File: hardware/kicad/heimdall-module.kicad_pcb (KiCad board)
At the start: 2 copper layers, 54.9 x 30.1 mm, 29 parts, among them J2 Breakout, U1 MC33269DT-3.3G, U2 ESP32-C3-WROOM-02-N4, U3 TYPEC-214-ARP14H105, U4 USBLC6-2SC6

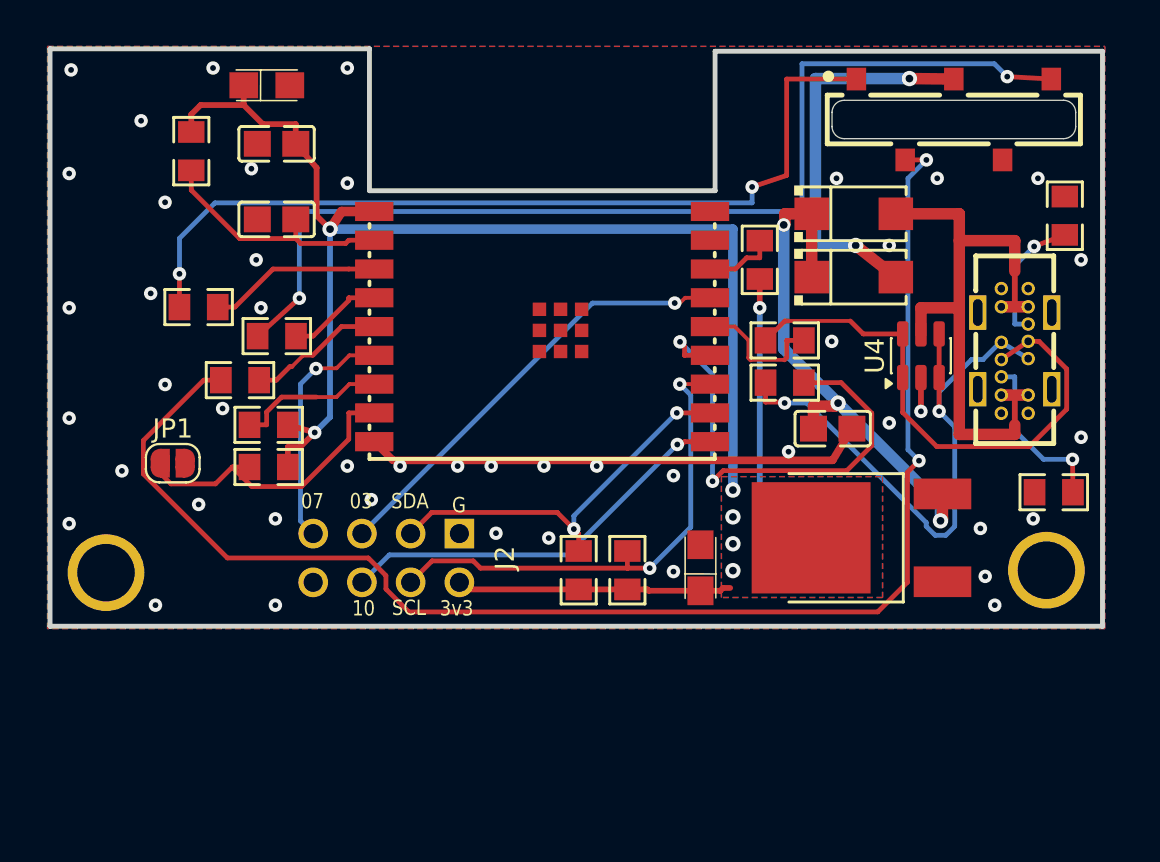
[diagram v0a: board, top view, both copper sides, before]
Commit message: Bay interface: Schottky isolation on all bay signal lines
The bay lines no longer connect straight to the ESP32 through 220R
(R5-R7 removed). Each line goes through a BAT54WS (D3-D6), the same
scheme as the DIY Multiprotocol module: the radio can only pull a line
low, and every high level comes from 3V3 pull-ups. A radio driving 5V
can't reach the ESP32.

- PPM in: D3 + R14 4.7k -> IO4
- DATA (CRSF, half duplex): RX D4 + R16 4.7k -> IO5, TX D5 <- IO6,
  R17 1.5k bay-side pull-up for fast rising edges
- HB out: D6 <- IO7, R15 4.7k bay-side pull-up
- Breakout J2 pin 7: IO7 -> IO1 (silk relabelled)

Board re-routed (prep -> Freerouting -> finish pipeline). DRC: 0 errors,
0 unconnected, 0 parity; only the known U3 A1 starved-thermal warning.

Co-Authored-By: Claude Opus 5.5 <noreply@anthropic.com>
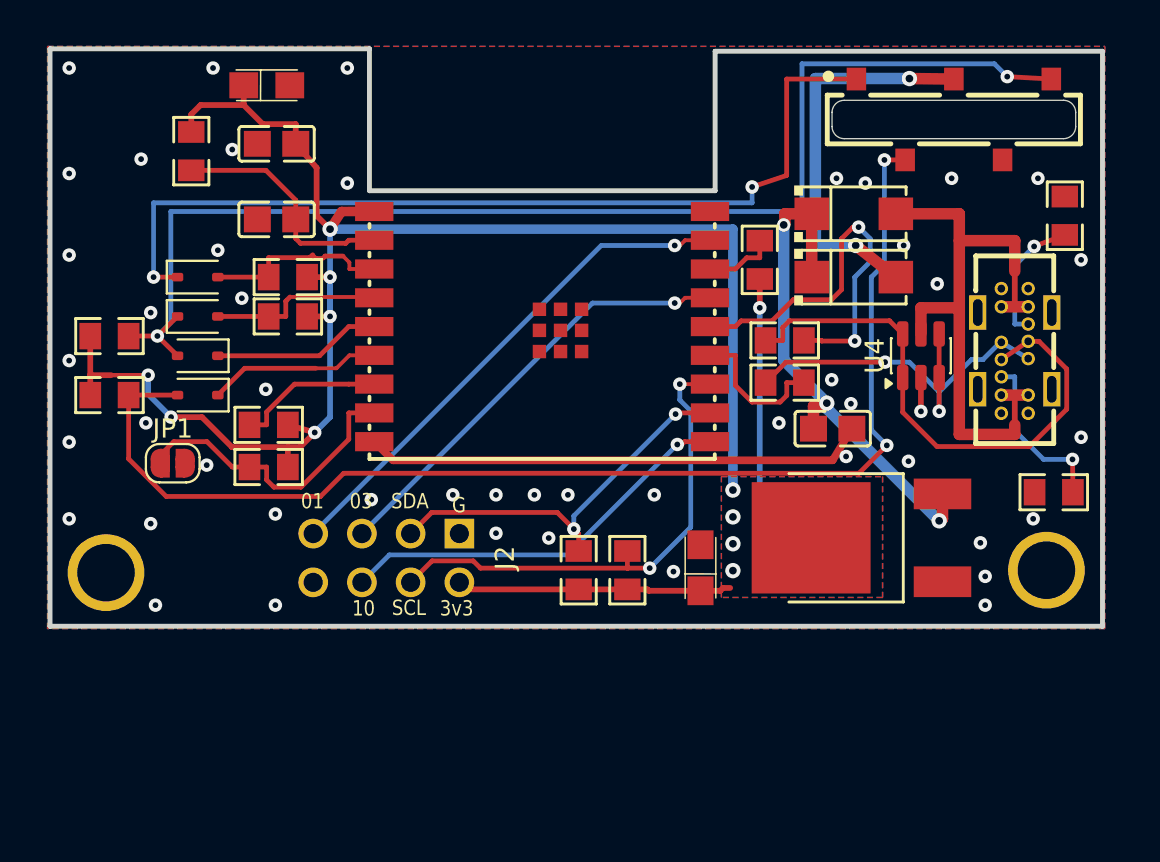
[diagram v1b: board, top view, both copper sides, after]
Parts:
- removed R5, R6, R7: 220Ω, heimdall-m-easyedapro:R0805
- added D3: BAT54WS, Diode_SMD:D_SOD-323, F.Cu at (127.7, 101.9)
- added D4: BAT54WS, Diode_SMD:D_SOD-323, F.Cu at (127.7, 104.0)
- added D5: BAT54WS, Diode_SMD:D_SOD-323, F.Cu at (127.7, 106.0)
- added D6: BAT54WS, Diode_SMD:D_SOD-323, F.Cu at (127.7, 108.0)
- added R14: 4.7kΩ, heimdall-m-easyedapro:R0805, F.Cu at (132.4, 101.9)
- added R15: 4.7kΩ, heimdall-m-easyedapro:R0805, F.Cu at (123.1, 108.0)
- added R16: 4.7kΩ, heimdall-m-easyedapro:R0805, F.Cu at (132.4, 104.0)
- added R17: 1.5kΩ, heimdall-m-easyedapro:R0805, F.Cu at (123.1, 105.0)
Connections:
- J2 pad 7: /IO7 -> /IO1
- U2 pad 17: unconnected-(U2-IO1-Pad17) -> /IO1
- U2 pad 3: Net-(U2-IO4) -> /PPM_IN
- U2 pad 4: Net-(U2-IO5) -> /DATA_RX
- U2 pad 5: Net-(U2-IO6) -> /DATA_TX
- U2 pad 6: /IO7 -> /HB_OUT
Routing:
- net /IO1: track 0.00 -> 27.0 mm, vias 0 -> 1
- net /VCC: track 91.7 -> 111.6 mm, vias 7 -> 11
- net Net-(U2-IO18): track 25.1 -> 7.64 mm, vias 2 -> 0
- net Net-(U2-IO19): track 7.09 -> 20.6 mm, vias 0 -> 2
- net /IO7: track 12.5 -> 0.00 mm, vias 1 -> 0
- net /HB: track 75.0 -> 63.9 mm
- net /DATA: track 54.6 -> 65.1 mm
- net /USB-D-: track 31.4 -> 21.1 mm
- net /PPM_IN: track 0.00 -> 9.82 mm
- net /DATA_RX: track 0.00 -> 9.08 mm
- net /HB_OUT: track 0.00 -> 9.01 mm
- net Net-(U2-IO4): track 8.98 -> 0.00 mm
- net /DATA_TX: track 0.00 -> 8.78 mm
- net Net-(U2-IO6): track 7.16 -> 0.00 mm
- net Net-(U2-IO5): track 4.99 -> 0.00 mm
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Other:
- board text added: "01"
- board text removed: "07"

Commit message: Bay DATA transmit through a 5V-tolerant buffer: S.Port and CRSF
The module has to talk S.Port (idle low, inverted) or CRSF (idle high)
on the DATA pin depending on what the internal module uses. The
pull-low-only diode and the 1.5k pull-up only worked for CRSF.

- D5 and the 1.5k pull-up out; U5 74LVC1G34 (always on) + R17 1k in.
  The UART idle level holds the line in either mode; the radio
  overrides 1k when it transmits.
- DATA_TX on IO7, HB_OUT on IO8 (R12 doubles as its pull-up), IO6 free.
- D6/R15 one step lower, R12/R13 0.3mm lower; DATA, HB, HB_OUT, D+/D-
  and the U5 supply hand-routed in route_pcb.py prep.

DRC: 0 unconnected, 0 parity. Two starved-thermal warnings: U3 A1 (as
before) and J2 pin 1 (plated through, connected on the bottom).

Co-Authored-By: Claude Opus 5.5 <noreply@anthropic.com>
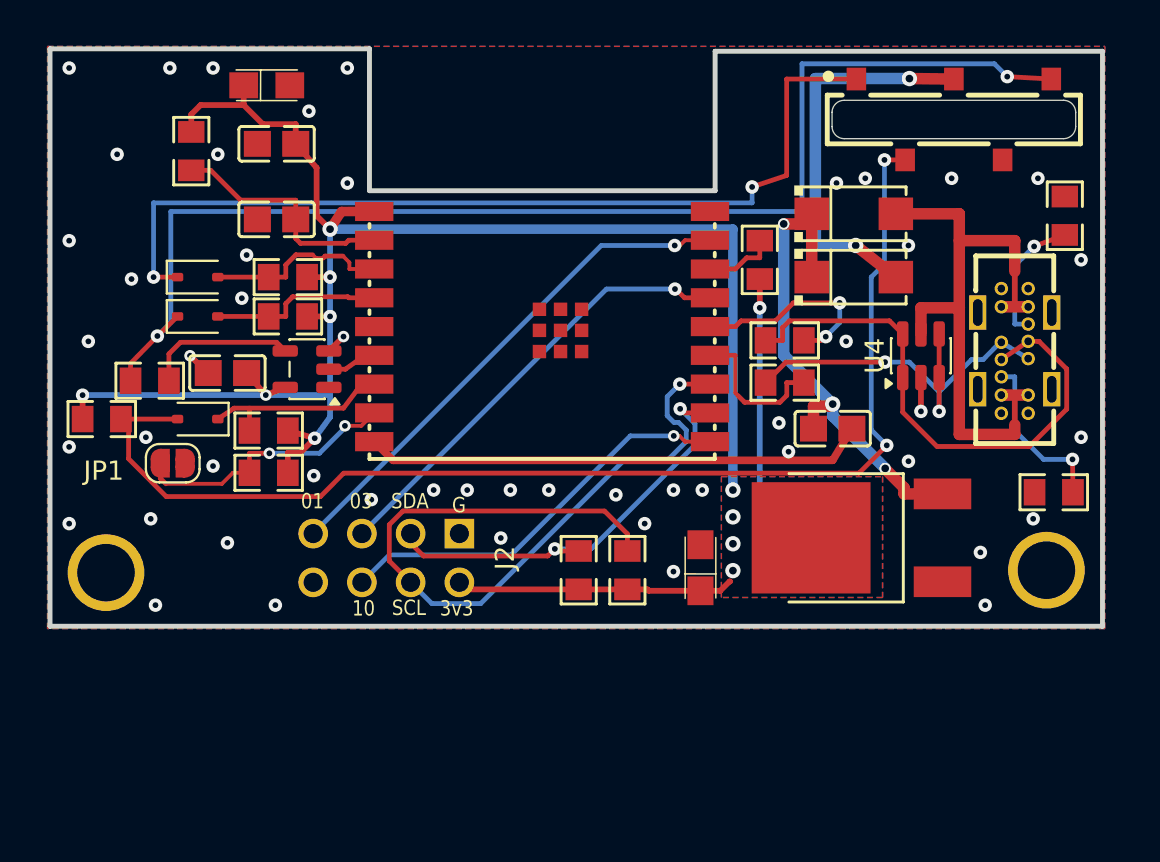
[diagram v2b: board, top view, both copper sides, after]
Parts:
- removed D5: BAT54WS, Diode_SMD:D_SOD-323
- added C6: 100nF, heimdall-m-easyedapro:C0805, F.Cu at (129.2, 106.9)
- added U5: 74LVC1G34, Package_TO_SOT_SMD:SOT-23-5, F.Cu at (133.4, 106.7)
- R17: value 1.5kΩ -> 1kΩ
- moved R17 3.13 mm to (125.2, 107.3)
- moved R15 1.31 mm to (122.7, 109.3)
- moved D6 1.25 mm to (127.7, 109.3)
- moved R12 0.30 mm to (131.4, 109.9)
- moved R13 0.30 mm to (131.4, 112.1)
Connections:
- R12 pad 1: /IO8 -> /HB_OUT
- R17 pad 1: /VCC -> /DATA
- R17 pad 2: /DATA -> /DATA_DRV
- U2 pad 5: /DATA_TX -> unconnected-(U2-IO6-Pad5)
- U2 pad 6: /HB_OUT -> /DATA_TX
- U2 pad 7: /IO8 -> /HB_OUT
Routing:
- net /SCL: track 26.3 -> 41.3 mm, vias 2 -> 1
- net Net-(U2-IO19): track 20.6 -> 10.6 mm
- net /DATA_DRV: track 0.00 -> 8.54 mm
- net /IO8: track 7.78 -> 0.00 mm
- net /DATA_TX: track 8.78 -> 2.56 mm
- net /SDA: track 20.6 -> 23.1 mm
- net GND: track 28.0 -> 30.4 mm, vias 48 -> 50
- net /VBAT: track 27.5 -> 25.7 mm
- net /IO9: track 15.6 -> 14.2 mm, vias 0 -> 2
- net /HB_OUT: track 9.01 -> 10.0 mm
- net /HB: track 63.9 -> 63.0 mm

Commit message: Fit the board to the Banggood 4-in-1 Multi case
Board outline = case cavity (57 x 41.5mm) - 0.3mm, notches for the latch
housings, M2 holes on the case's three standoffs (copper kept 2mm clear),
measured from MULTI-Module_Bangood_4-in-1_Case.stl.

- H1 + slot moved 1.25mm towards the end wall and 0.25mm towards the case
  centre: the bay pin position three JR-bay designs agree on (Multi
  STM32 v1.0t Eagle, Multipro V2 Gerbers, ELRS TX_SX1280 Gerbers)
- module and left side 2.8mm down (antenna end clears the latch housing),
  USB/ESD/diodes 3.7mm down, U1 also 4.1mm right, C2 beside U1's tab,
  R1/R2 moved; MH1/MH2 replaced by MH1-MH3 on the standoffs
- route_pcb.py prep draws hand routes per placement group; the bay lines
  from H1, CC1/CC2, 3V3 trunk start, GND spine and HB are redrawn
- case_place.py: the placement step

DRC: 0 unconnected, 0 parity; starved-thermal warnings on U3 A1 and J2
pin 1 as before.

Co-Authored-By: Claude Opus 5.5 <noreply@anthropic.com>
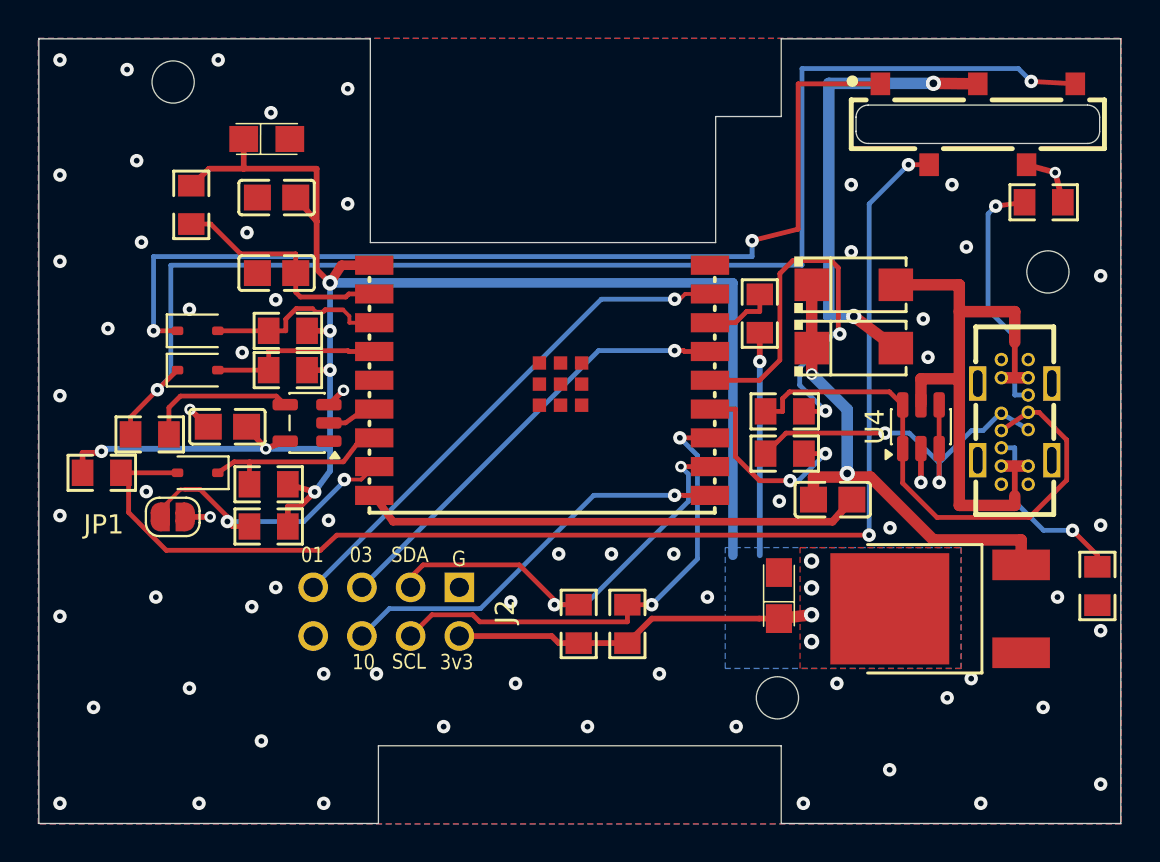
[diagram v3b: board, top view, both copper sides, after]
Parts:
- added MH3: M2, MountingHole:MountingHole_2.2mm_M2, F.Cu at (157.9, 123.8)
- MH1: value (none) -> M2; footprint Pad_e163 -> MountingHole:MountingHole_2.2mm_M2
- MH2: value (none) -> M2; footprint Pad_e6 -> MountingHole:MountingHole_2.2mm_M2
- moved MH1 25.8 mm to (126.4, 91.7)
- moved MH2 15.5 mm to (172.0, 101.6)
- moved U1 5.52 mm to (167.2, 119.2)
- moved R2 5.39 mm to (174.6, 118.0), turned to 90 degrees
- moved C2 4.34 mm to (158.0, 118.5)
- moved C1 3.70 mm to (160.8, 113.5)
- moved D1 3.70 mm to (161.9, 102.3)
- moved R3 3.70 mm to (158.3, 108.9)
- moved U4 3.70 mm to (165.4, 109.7)
- moved D2 3.70 mm to (161.9, 105.6)
- moved R4 3.70 mm to (158.3, 111.1)
- moved U3 3.70 mm to (170.3, 109.4)
- moved JP1 2.80 mm to (126.4, 114.4)
- moved R13 2.80 mm to (131.4, 114.9)
- moved U2 2.80 mm to (145.7, 107.3)
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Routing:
- net /SCL: track 41.3 -> 25.7 mm, vias 1 -> 2
- net Net-(U2-IO19): track 10.6 -> 22.3 mm
- net /VCC: track 111.2 -> 119.4 mm
- net Net-(U3-CC2): track 6.88 -> 12.8 mm
- net GND: track 30.4 -> 34.7 mm, vias 50 -> 66
- net /DATA: track 65.0 -> 68.8 mm
- net /SIGNAL: track 47.7 -> 51.5 mm
- net /VBAT_IN: track 20.7 -> 24.0 mm
- net /HB: track 63.0 -> 66.0 mm
- net Net-(U2-IO18): track 7.88 -> 10.7 mm, vias 0 -> 2
- net /IO9: track 14.2 -> 15.3 mm
- net Net-(U3-CC1): track 8.85 -> 9.57 mm
- net /DATA_DRV: track 8.54 -> 7.89 mm
- net /VBAT: track 25.7 -> 25.4 mm, vias 3 -> 2
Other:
- board size 54.9 x 30.1 mm -> 56.4 x 40.9 mm

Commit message: Mounting holes for M3 instead of M2
MH1-MH3: MountingHole_3.2mm_M3_ISO14580 (5.5mm head), copper kept 3mm
clear. To make room at MH2/MH3: R1 moved left of H1's pin 4, CC2 and the
VBUS exit rerouted round the hole, USB group 0.3mm lower (GND spine and HB
follow), U1 0.5mm further right with the heatsink copper widened, R9/R10
VCC hand-routed into the bottom heatsink copper.

DRC: 0 unconnected, 0 parity; starved-thermal warnings on U3 A1 and J2
pin 1 as before.

Co-Authored-By: Claude Opus 5.5 <noreply@anthropic.com>
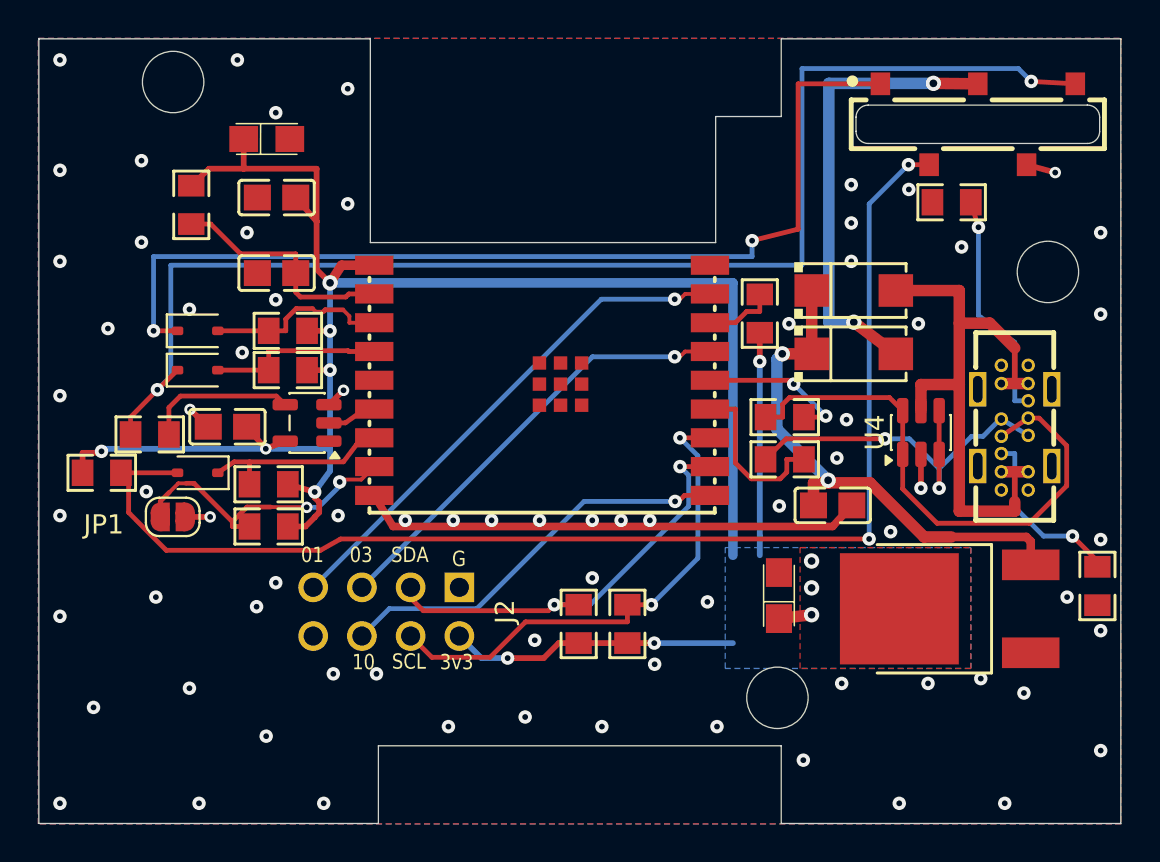
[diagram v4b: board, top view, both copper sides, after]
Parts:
- MH1, MH2, MH3: value M2 -> M3; footprint MountingHole:MountingHole_2.2mm_M2 -> MountingHole:MountingHole_3.2mm_M3_ISO14580
- moved R1 4.80 mm to (167.0, 98.0), turned to 180 degrees
- moved U1 0.50 mm to (167.7, 119.2)
- moved D2 0.30 mm to (161.9, 105.9)
- moved R4 0.30 mm to (158.3, 111.4)
- moved U3 0.30 mm to (170.3, 109.7)
- moved C1 0.30 mm to (160.8, 113.8)
- moved D1 0.30 mm to (161.9, 102.6)
- moved R3 0.30 mm to (158.3, 109.2)
- moved U4 0.30 mm to (165.4, 110.0)
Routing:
- net Net-(U2-IO19): track 22.3 -> 7.97 mm
- net /VBAT: track 25.4 -> 27.8 mm
- net /VCC: track 119.4 -> 117.5 mm, vias 11 -> 12
- net Net-(U2-IO18): track 10.7 -> 8.86 mm, vias 2 -> 0
- net GND: track 34.7 -> 33.3 mm, vias 66 -> 74
- net /VBUS: track 32.3 -> 31.2 mm
- net Net-(U3-CC2): track 12.8 -> 12.1 mm
- net /SDA: track 23.4 -> 22.7 mm
- net /SCL: track 25.7 -> 26.3 mm
